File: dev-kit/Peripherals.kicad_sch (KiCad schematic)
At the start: 44 parts, among them IC201 APDS-9306-065, IC202 BMI270, IC203 BMP581, IC204 LIS2MDLTR, IC306 DRV2603RUNT, IC307 RV-8263-C8, M302 Vibrator DC Motor, Q201 DMG1013UW-7, Q301 BC817W, Q302 PMZ550UNEYL, Q303 PMZ550UNEYL, X102 MOTOR

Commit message: Working on the layout for the dev kit
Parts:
- added TP111: VIB-PWM, TestPoint:TestPoint_Pad_D1.0mm, symbol Connector:TestPoint
- added TP112: VIB-EN, TestPoint:TestPoint_Pad_D1.0mm, symbol Connector:TestPoint
- C208: footprint Capacitor_SMD:C_0603_1608Metric -> Capacitor_SMD:C_0402_1005Metric; manf# 06033C224KAT2A -> 04023C224KAT2A; mouser# 581-06033C224KAT2A -> 581-04023C224KAT2A
- R201: footprint Resistor_SMD:R_0603_1608Metric -> Resistor_SMD:R_0402_1005Metric; manf# RC0603FR-07150KL -> RC0404FR-07150KL; mouser# 603-RC0603FR-07150KL -> 603-RC0404FR-07150KL
- X102: value MOTOR -> Motor
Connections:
- net +1V8: now also R122.1; no longer Q201.2 (S), R201.2
- net VIB-EN: now also TP112.1
- net VIB-PWM: now also TP111.1
- net at X102.1 (Pin_1): now also IC306.6 (OUT-); no longer IC306.9 (OUT+)
- net at X102.2 (Pin_2): now also IC306.9 (OUT+); no longer IC306.6 (OUT-)
- net at C204.1, Q201.3 (D): now also MK201.4 (VDD); no longer R122.1
- net APDS-INT: now reaches IC201.4 (INT)
- net at R122.2: now also Q201.2 (S), R201.2; no longer MK201.4 (VDD)
- net BMI270-INT1 renamed BMI270-INT
- net BMI270-INT2: no longer names the net of IC202.9 (INT2)
- net nRTC-INT renamed ~{RTC-INT}
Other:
- moved on the sheet: BZ301, D301, Q201, R122, R201, R307, R311, S301, S302, S303, S304

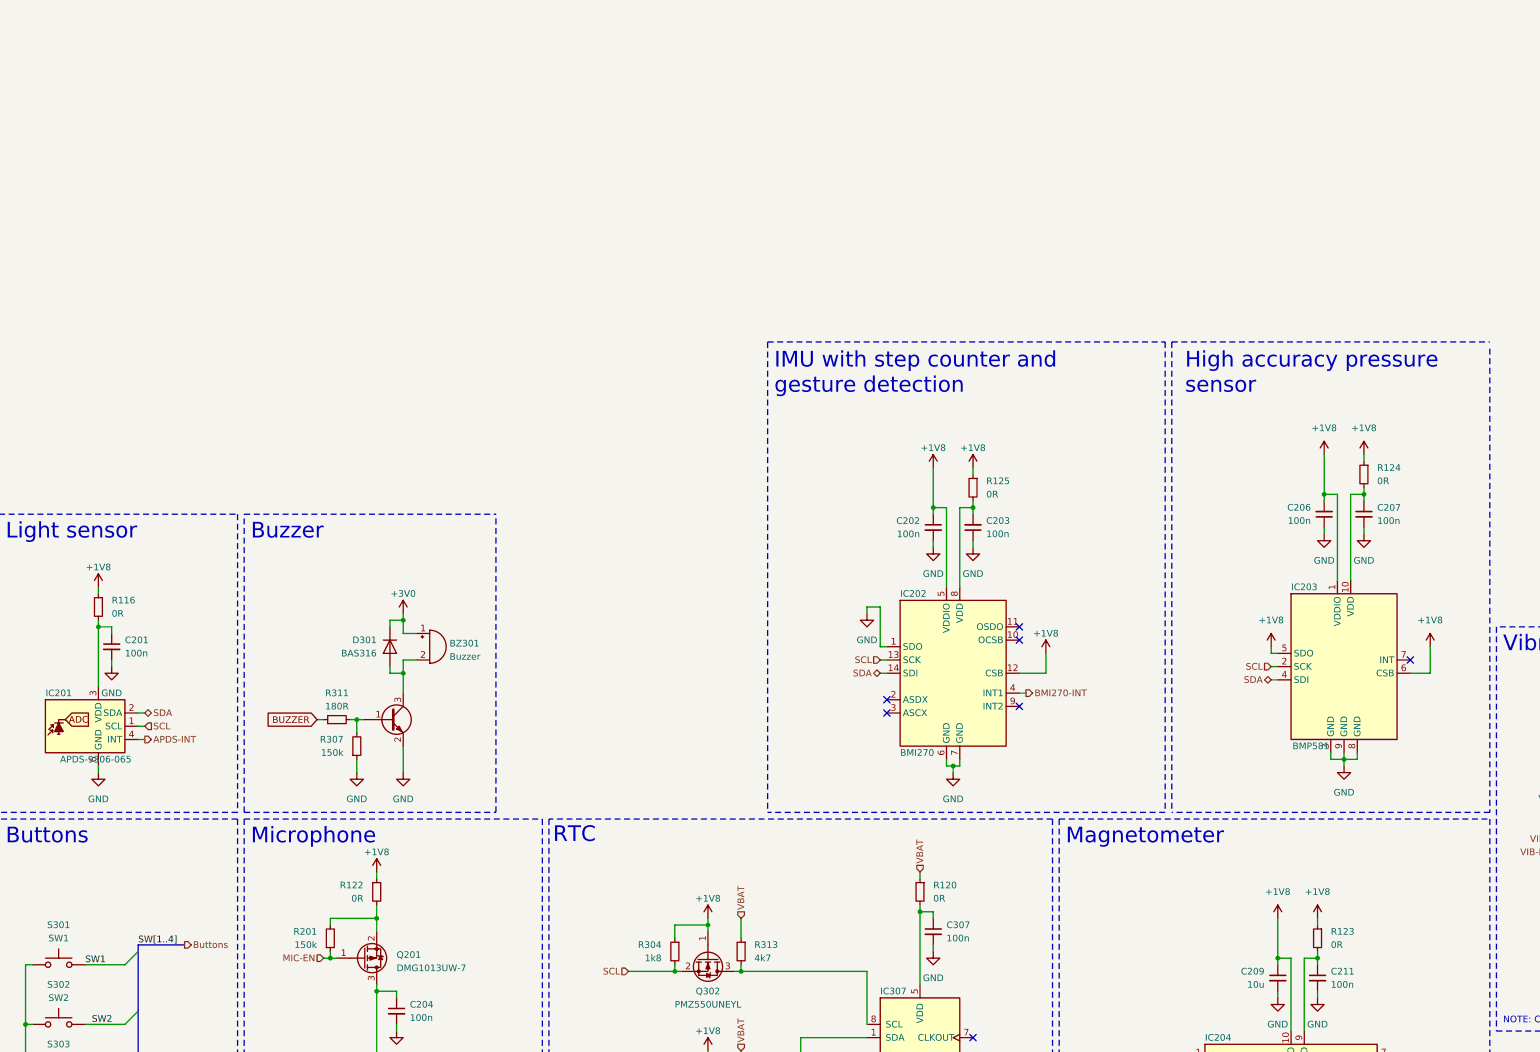
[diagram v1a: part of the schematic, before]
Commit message: Add more documentation
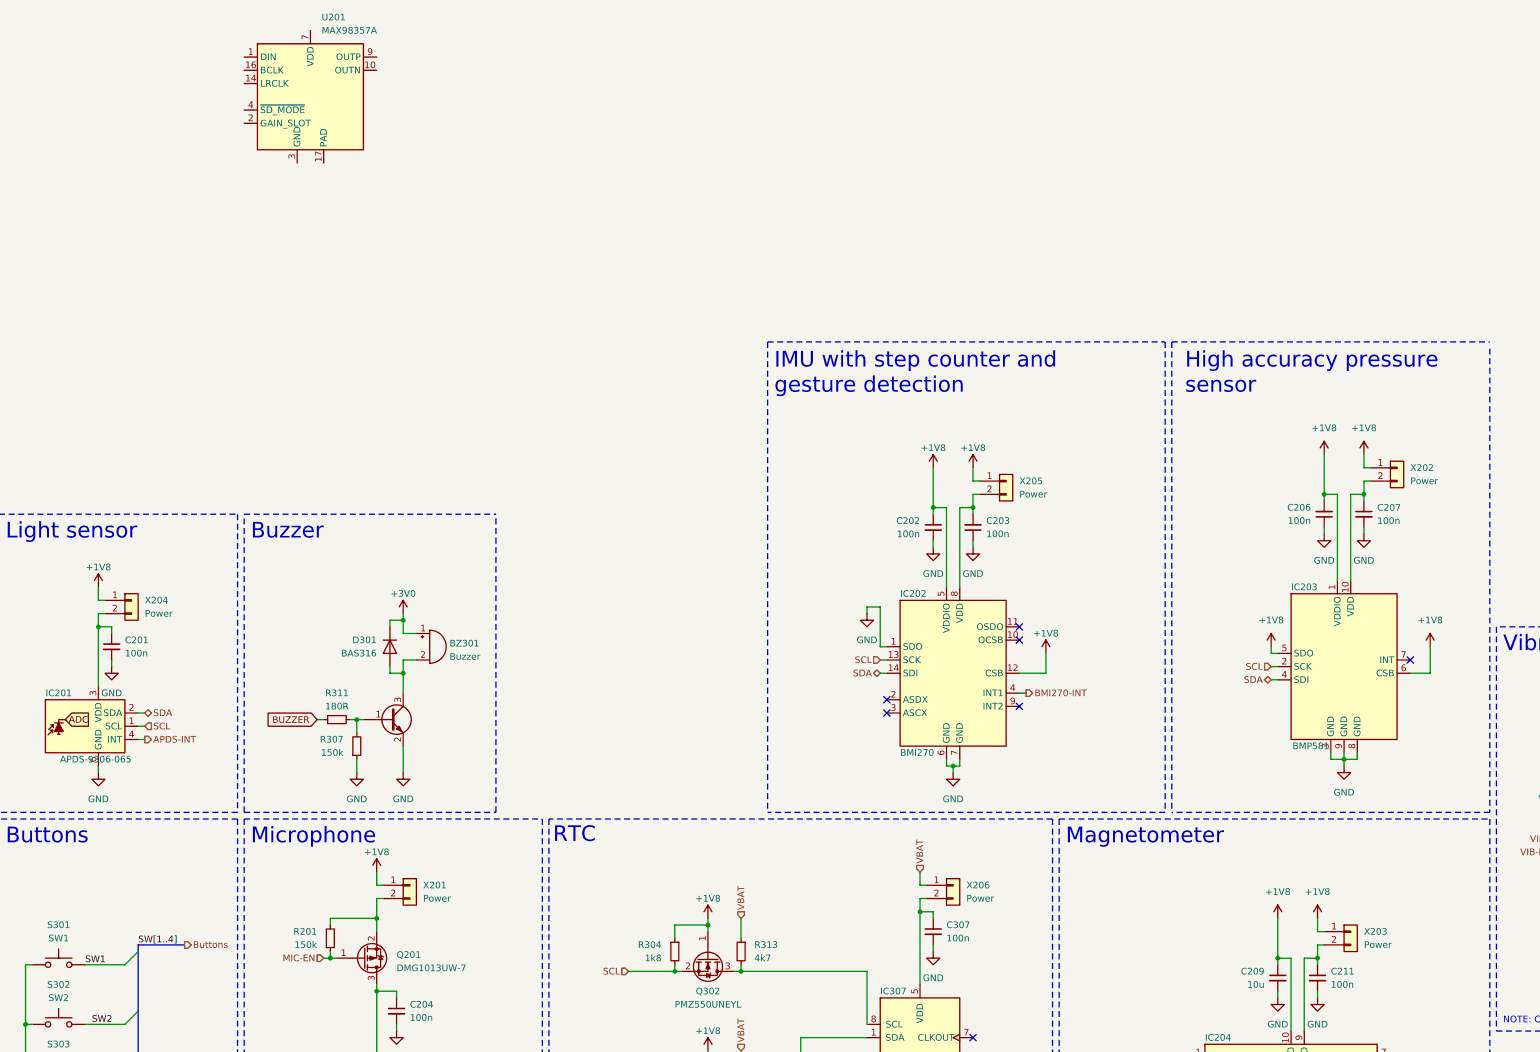
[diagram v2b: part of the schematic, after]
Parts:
- removed R116, R120, R122, R123, R124, R125: 0R, Resistor_SMD:R_0805_2012Metric, symbol Device:R_Small
- added U201: MAX98357A, Package_DFN_QFN:TQFN-16-1EP_3x3mm_P0.5mm_EP1.23x1.23mm, symbol Audio:MAX98357A
- added X201, X202, X203, X204, X205, X206: Power, Connector_PinHeader_2.54mm:PinHeader_1x02_P2.54mm_Vertical_SMD_Pin1Left, symbol Connector_Generic:Conn_01x02
- S301, S302, S303, S304: footprint E-Switch:TL6340AF160Q_Modified -> Wuerth:WS-TASV-6x6; manf E-Switch -> Wurth Elektronik; manf# TL6340AF160Q -> 430182050816; mouser# 612-TL6340AF160Q -> 710-430182050816
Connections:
- net +1V8: now also X201.1 (Pin_1), X202.1 (Pin_1), X203.1 (Pin_1), X204.1 (Pin_1), X205.1 (Pin_1)
- net VBAT: now also X206.1 (Pin_1)
- net at C211.1, IC204.9 (VDD): now also X203.2 (Pin_2)
- net at C307.1, IC307.5 (VDD): now also X206.2 (Pin_2)
- net at C207.1, IC203.10 (VDD): now also X202.2 (Pin_2)
- net at C203.2, IC202.8 (VDD): now also X205.2 (Pin_2)
- net at C201.1, IC201.3 (VDD): now also X204.2 (Pin_2)
- net at Q201.2 (S), R201.2: now also X201.2 (Pin_2)
- new net: U201.11 (GND), U201.15 (GND), U201.3 (GND)
- new net: U201.7 (VDD), U201.8 (VDD)

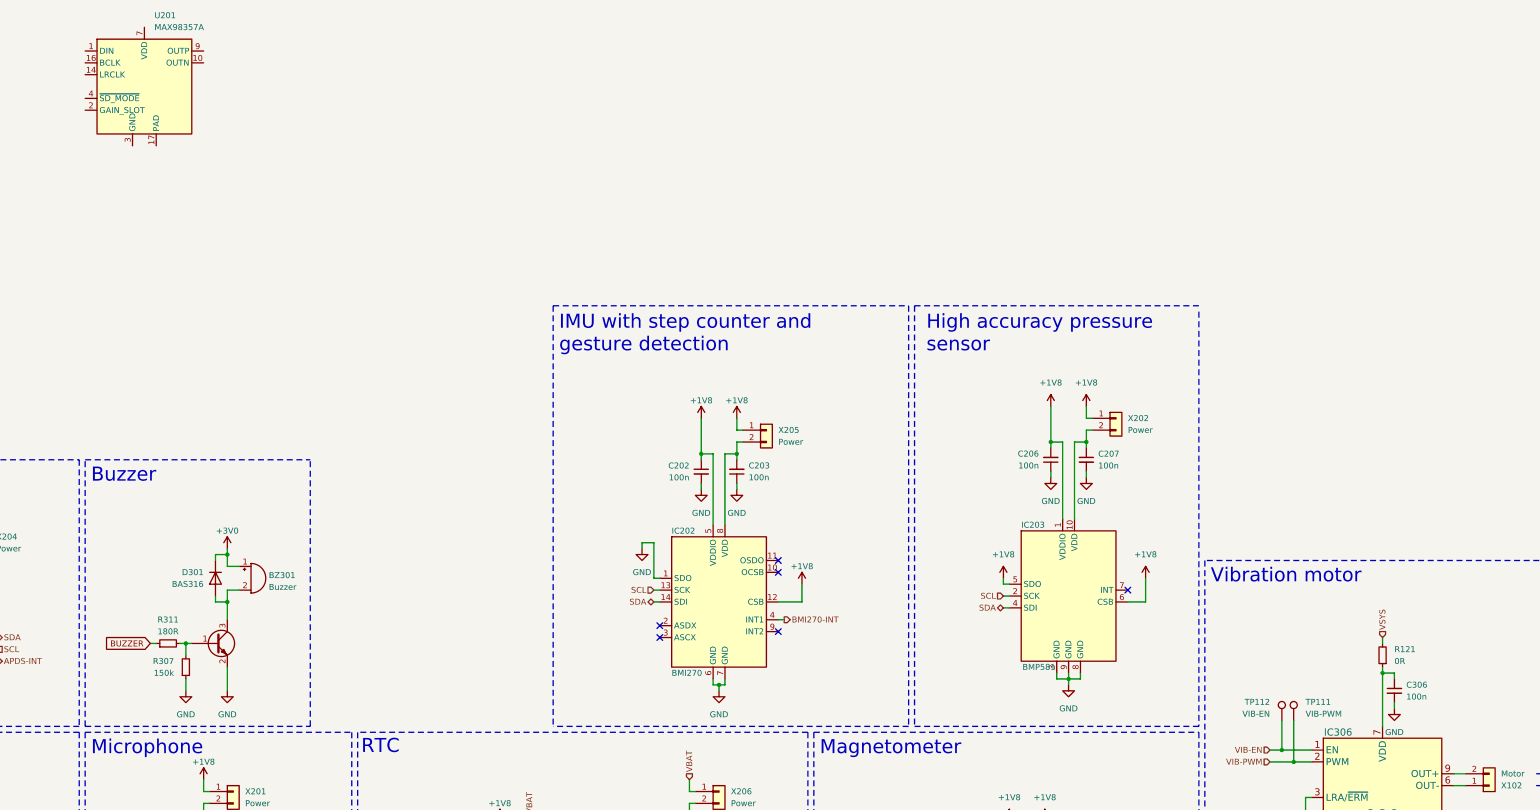
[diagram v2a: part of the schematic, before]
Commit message: Add CI/CD pipeline for Dev-Kit, more Dev-Kit improvements
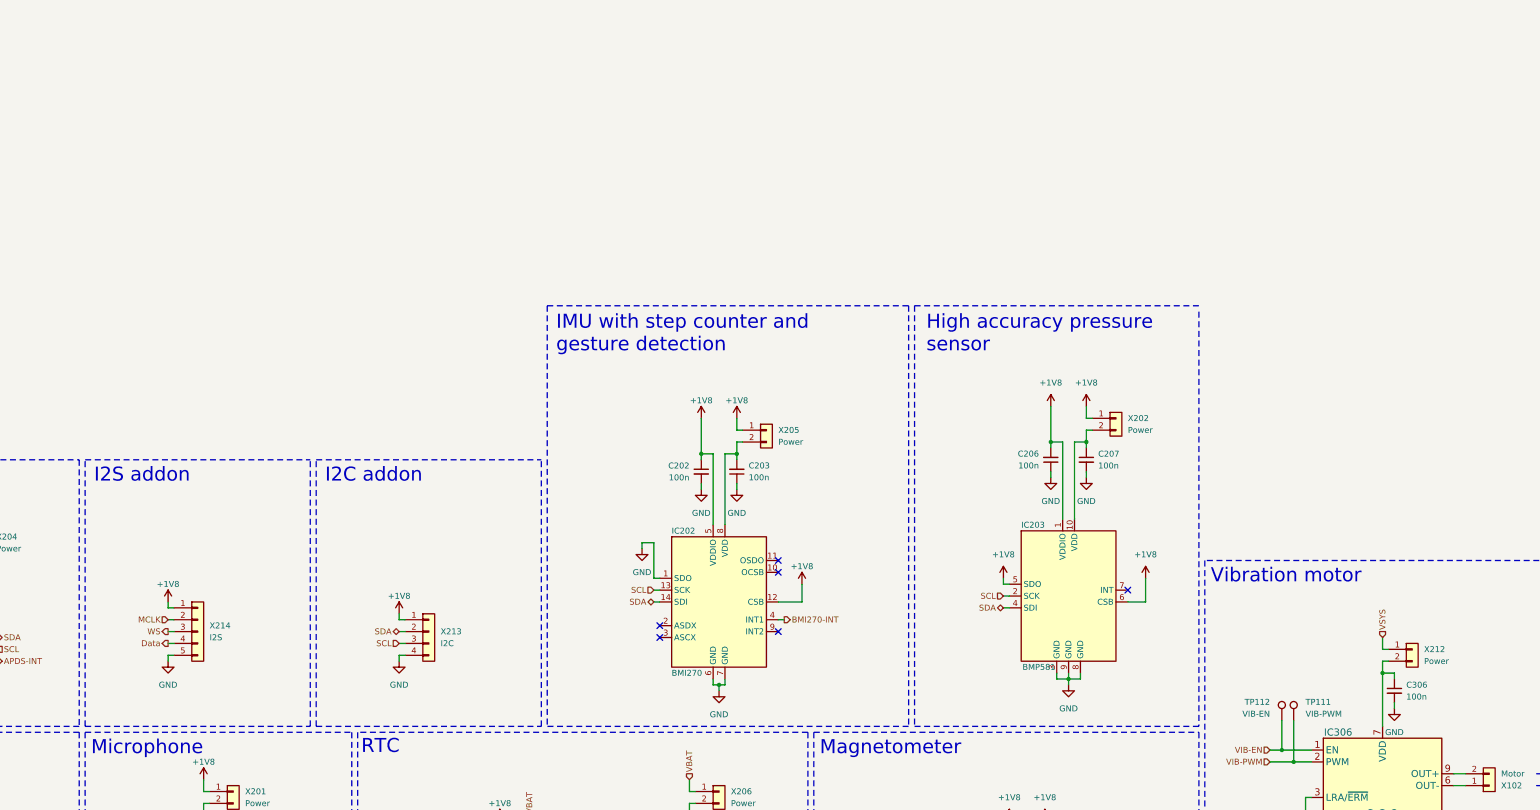
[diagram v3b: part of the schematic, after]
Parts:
- removed BZ301: Buzzer, CUI Devices:CMT-322-65-SMT-TR, symbol Device:Buzzer
- removed D301: BAS316, Diode_SMD:D_SOD-323, symbol Diode:BAS316
- removed Q301: BC817W, Package_TO_SOT_SMD:SOT-323_SC-70, symbol Transistor_BJT:BC817W
- removed R121: 0R, Resistor_SMD:R_0805_2012Metric, symbol Device:R_Small
- removed R307: 150k, Resistor_SMD:R_0603_1608Metric, symbol Device:R_Small
- removed R311: 180R, Resistor_SMD:R_0603_1608Metric, symbol Device:R_Small
- removed U201: MAX98357A, Package_DFN_QFN:TQFN-16-1EP_3x3mm_P0.5mm_EP1.23x1.23mm, symbol Audio:MAX98357A
- added X212: Power, Connector_PinHeader_2.54mm:PinHeader_1x02_P2.54mm_Vertical_SMD_Pin1Left, symbol Connector_Generic:Conn_01x02
- added X213: I2C, Connector_PinHeader_2.54mm:PinHeader_1x04_P2.54mm_Vertical_SMD_Pin1Left, symbol Connector_Generic:Conn_01x04
- added X214: I2S, Connector_PinHeader_2.54mm:PinHeader_1x05_P2.54mm_Vertical_SMD_Pin1Left, symbol Connector_Generic:Conn_01x05
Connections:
- net +1V8: now also X213.1 (Pin_1), X214.1 (Pin_1)
- net GND: now also X213.4 (Pin_4), X214.5 (Pin_5)
- net SCL: now also X213.3 (Pin_3)
- net SDA: now also X213.2 (Pin_2)
- net VSYS: now also X212.1 (Pin_1)
- net at C306.1, IC306.7 (VDD): now also X212.2 (Pin_2)
- new net Data: X214.4 (Pin_4)
- new net MCLK: X214.2 (Pin_2)
- new net WS: X214.3 (Pin_3)
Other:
- note added: "I2C addon"
- note added: "I2S addon"
- note removed: "Buzzer"

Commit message: Changes from Jacob
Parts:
- X202: renamed from X214; manf (none) -> Amphenol FCI; manf# (none) -> 10129380-905002ALF; mouser# (none) -> 649-10129380-905002ALF
- X204: renamed from X213; manf (none) -> Amphenol FCI; manf# (none) -> 10129380-904002ALF; mouser# (none) -> 649-10129380-904002ALF
- renumbered C204 to C202, C202 to C203, C307 to C204, C203 to C205, C208 to C206, C209 to C207, C211 to C208, C206 to C209, C207 to C210, C306 to C211, IC307 to IC202, IC202 to IC203, IC203 to IC205, IC306 to IC206, M302 to M201, Q302 to Q202, Q303 to Q203, R304 to R202, R303 to R203, R313 to R204, R309 to R205, S301 to S201, S302 to S202, S303 to S203, S304 to S204, TP112 to TP201, TP111 to TP202, X204 to X201, X201 to X203, X206 to X205, X205 to X206, X203 to X207, X202 to X208, X212 to X209, X102 to X210

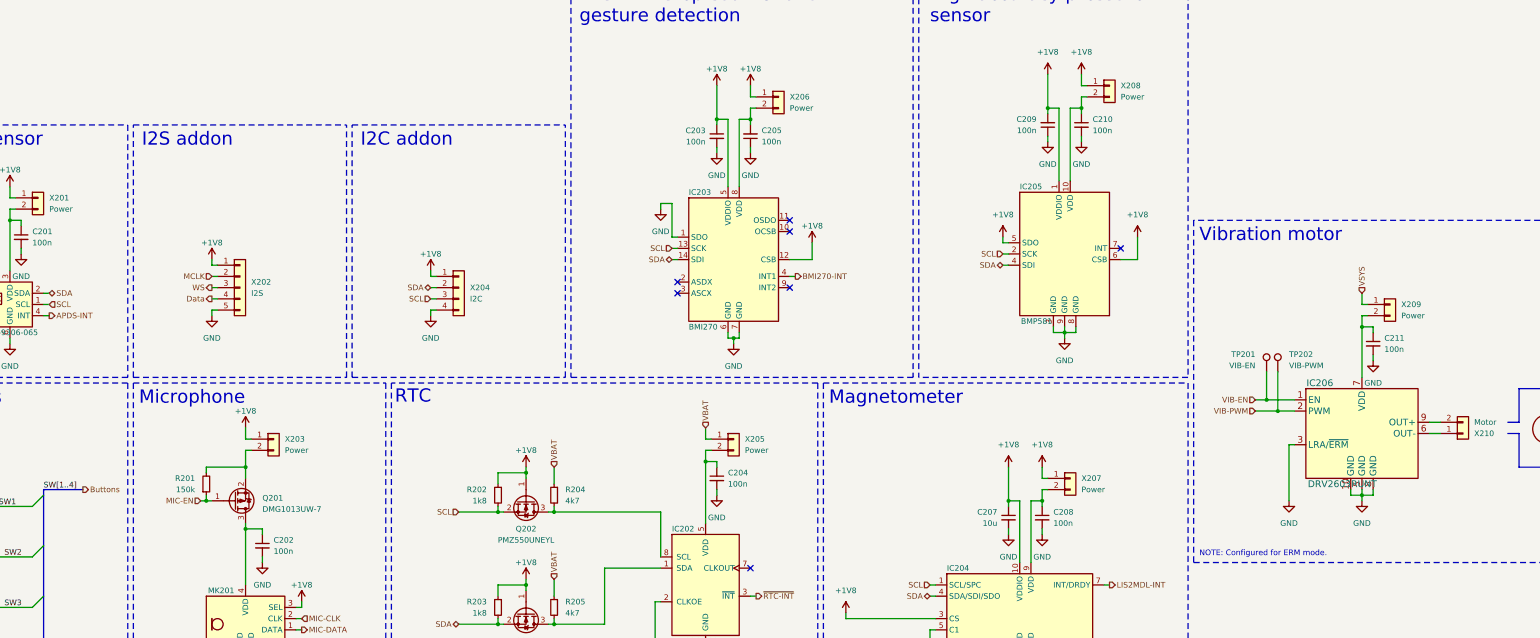
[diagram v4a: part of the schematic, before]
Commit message: Add impedance matching for USB, add jumper caps
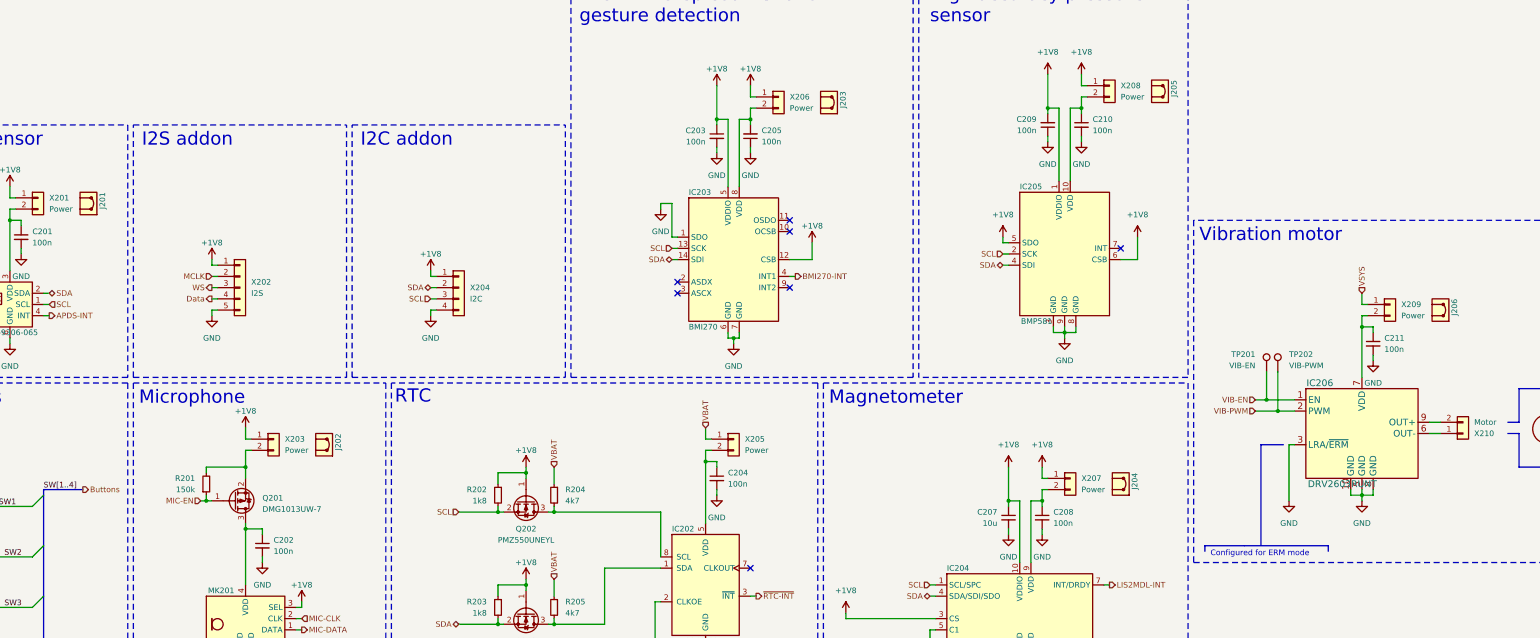
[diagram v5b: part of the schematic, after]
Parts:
- added J201, J202, J203, J204, J205, J206: Jumper, symbol Misc:Jumper
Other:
- note added: "Configured for ERM mode"
- note removed: "NOTE: Configured for ERM mode."
- title: ZSWatch v3 Dev-Kit -> https://github.com/ZSWatch/Watch-HW

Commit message: Cosmetic changes
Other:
- company: github.com/jakkra/ZSWatch-HW -> https://github.com/ZSWatch/Watch-HW
- title: https://github.com/ZSWatch/Watch-HW -> Watch-HW
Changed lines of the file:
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@@
 	(paper "A3")
 	(title_block
-		(title "https://github.com/ZSWatch/Watch-HW")
+		(title "Watch-HW")
 		(date "2025-05-09")
 		(rev "0")
-		(company "github.com/jakkra/ZSWatch-HW")
+		(company "https://github.com/ZSWatch/Watch-HW")
 	)
 	(text "Vibration motor"

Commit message: Fix wrong part number for R102 and R201
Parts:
- R201: manf# RC0404FR-07150KL -> RC0402FR-07150KL
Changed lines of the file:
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@@
 			)
 		)
-		(property "manf#" "RC0404FR-07150KL"
+		(property "manf#" "RC0402FR-07150KL"
 			(at 76.2 233.68 0)
 			(effects
